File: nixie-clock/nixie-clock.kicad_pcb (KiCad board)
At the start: 2 copper layers, 184 x 105 mm, 63 parts, among them J1 Barrel_Jack_Switch, J2 Conn_01x08, J3 Conn_01x06, J4 AVR-ISP-6, SW1 SW_Push, SW2 SW_Push, SW3 SW_Push, SW4 SW_Push, U1 NCH6100HV, U10 74HC595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

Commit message: Add some extra silkscreen stuff.
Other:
- board text added: "IN-1"
- board text added: "IN-12"
- board text added: "IN-2"
- board text added: "IN-3"
- board text added: "IN1, IN12, IN2, IN3 Nixie Clock Nathan Aquino Dornback ndornback@gmail.com April 24th, 2020"
- board text removed: "IN1, IN12, IN2, IN3 Nixie Clock Nathan Aquino Dornback April 24th, 2020"
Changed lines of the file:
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@@
   (general
     (thickness 1.6)
-    (drawings 67)
+    (drawings 75)
     (tracks 1456)
     (zones 0)
@@
     (39 F.Mask user)
     (40 Dwgs.User user)
-    (41 Cmts.User user hide)
+    (41 Cmts.User user)
     (42 Eco1.User user)
     (43 Eco2.User user)
@@
       (effects (font (size 1.27 1.27) (thickness 0.1016)))
     )
-    (fp_text value IN-3 (at 0 0) (layer F.SilkS)
+    (fp_text value IN-3 (at 0 -5) (layer F.SilkS) hide
       (effects (font (size 1.27 1.27) (thickness 0.15)))
     )
@@
       (effects (font (size 1.27 1.27) (thickness 0.1016)))
     )
-    (fp_text value IN-3 (at 0 0) (layer F.SilkS)
+    (fp_text value IN-3 (at 0 0) (layer F.SilkS) hide
       (effects (font (size 1.27 1.27) (thickness 0.15)))
     )
@@
       (effects (font (size 1.27 1.27) (thickness 0.1016)))
     )
-    (fp_text value IN-12A (at 0 0) (layer F.SilkS)
+    (fp_text value IN-12A (at 0 -4.129158) (layer F.SilkS) hide
       (effects (font (size 1.27 1.27) (thickness 0.15)))
     )
-    (fp_text user Top (at 0.635 -5.715) (layer F.SilkS)
-      (effects (font (size 1.27 1.27) (thickness 0.1016)))
-    )
-    (fp_text user Bot (at 0.635 5.715) (layer F.SilkS)
+    (fp_text user Bot (at 0.225567 5.715) (layer F.SilkS)
       (effects (font (size 1.27 1.27) (thickness 0.1016)))
     )
@@
       (effects (font (size 1.27 1.27) (thickness 0.1016)))
     )
-    (fp_text value IN-12A (at 0 0) (layer F.SilkS)
+    (fp_text value IN-12A (at 0 0) (layer F.SilkS) hide
       (effects (font (size 1.27 1.27) (thickness 0.15)))
     )
-    (fp_text user Top (at 0.635 -5.715) (layer F.SilkS)
-      (effects (font (size 1.27 1.27) (thickness 0.1016)))
-    )
-    (fp_text user Bot (at 0.635 5.715) (layer F.SilkS)
+    (fp_text user Bot (at 0.135567 5.715) (layer F.SilkS)
       (effects (font (size 1.27 1.27) (thickness 0.1016)))
     )
@@
     )
   )
+  (gr_text IN-3 (at 166 101.5) (layer F.SilkS)
+    (effects (font (size 1 1) (thickness 0.15)))
+  )
+  (gr_text IN-3 (at 114 101.5) (layer F.SilkS)
+    (effects (font (size 1 1) (thickness 0.15)))
+  )
+  (gr_text IN-12 (at 129.5 110.5) (layer F.SilkS)
+    (effects (font (size 1 1) (thickness 0.15)))
+  )
+  (gr_text IN-12 (at 150.5 110.5) (layer F.SilkS)
+    (effects (font (size 1 1) (thickness 0.15)))
+  )
+  (gr_text IN-1 (at 88 115) (layer F.SilkS)
+    (effects (font (size 3 3) (thickness 0.45)))
+  )
+  (gr_text IN-1 (at 50 115) (layer F.SilkS)
+    (effects (font (size 3 3) (thickness 0.45)))
+  )
+  (gr_text IN-2 (at 199 115) (layer F.SilkS)
+    (effects (font (size 1 1) (thickness 0.15)))
+  )
+  (gr_text IN-2 (at 180 115) (layer F.SilkS)
+    (effects (font (size 1 1) (thickness 0.15)))
+  )
   (dimension 105 (width 0.15) (layer Dwgs.User)
     (gr_text "105.000 mm" (at 217.3 82.5 90) (layer Dwgs.User)
@@
     (arrow2b (pts (xy 124 131) (xy 125.126504 130.413579)))
   )
-  (gr_text "IN1, IN12, IN2, IN3 Nixie Clock\nNathan Aquino Dornback\nApril 24th, 2020" (at 203 126) (layer B.SilkS)
+  (gr_text "IN1, IN12, IN2, IN3 Nixie Clock\nNathan Aquino Dornback\nndornback@gmail.com\nApril 24th, 2020\n" (at 203 126) (layer B.SilkS)
     (effects (font (size 1 1) (thickness 0.15)) (justify left mirror))
   )

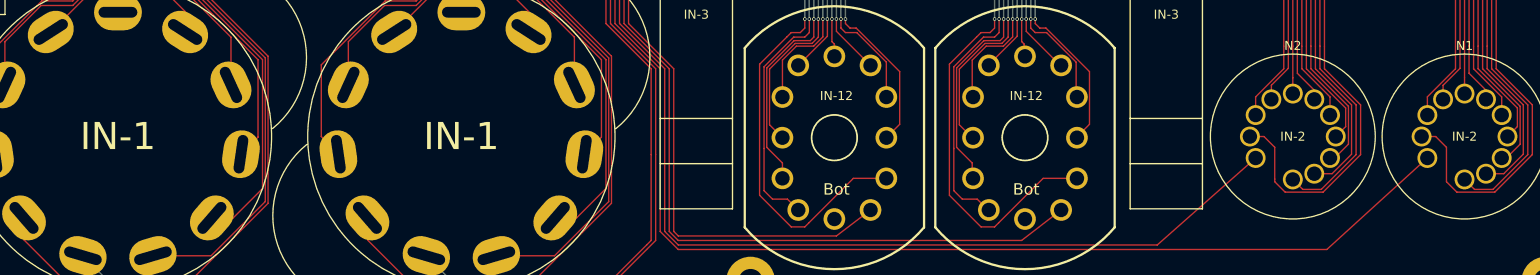
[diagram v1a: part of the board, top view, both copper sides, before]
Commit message: Added several image footprints. Added to nixie-clock silkscreen.
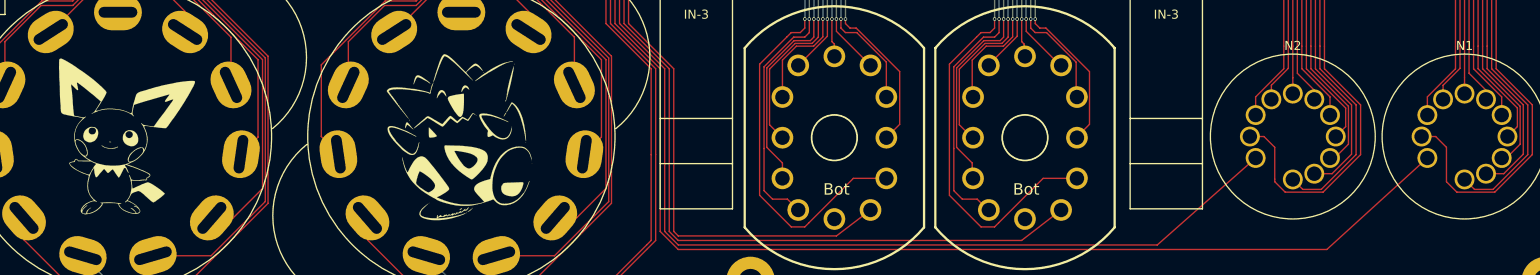
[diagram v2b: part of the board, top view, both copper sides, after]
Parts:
- added G***: LOGO, footprints-nad:pichu1, F.Cu at (51.0, 115.0)
- added G***: LOGO, footprints-nad:togepi1, F.Cu at (88.0, 115.0)

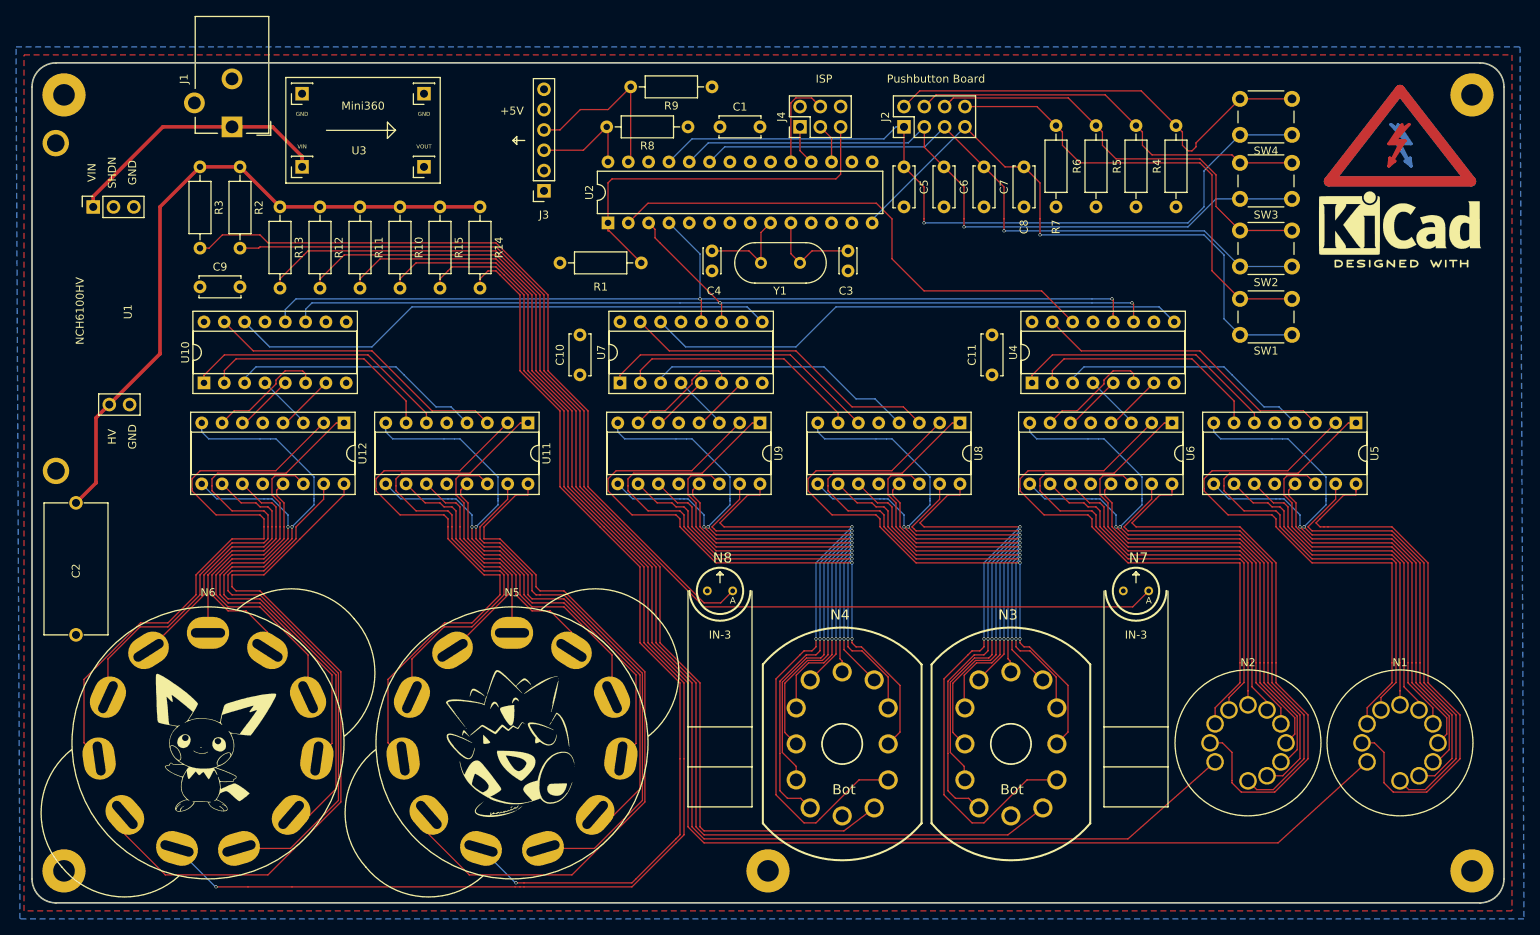
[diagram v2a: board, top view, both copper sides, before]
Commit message: Added res/cap values to silkscreen and more adjustments. Added footprint-tester board sent to OSHPARK.
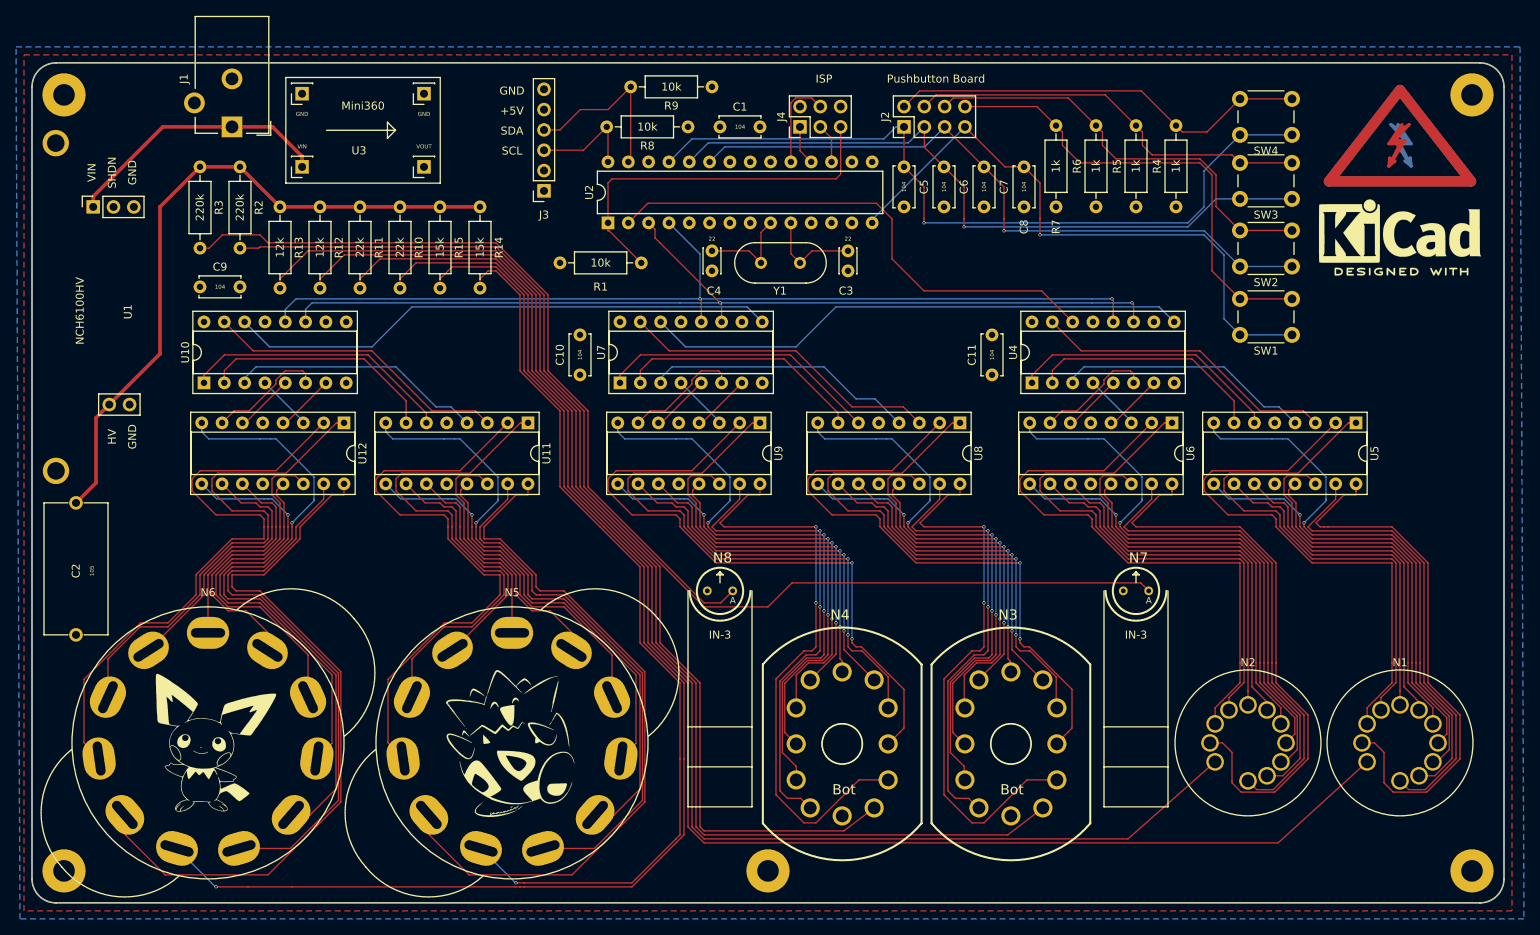
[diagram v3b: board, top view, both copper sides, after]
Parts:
- moved REF** 1.00 mm to (199.0, 51.0)
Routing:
- net /shiftout/N3_0: track 76.3 -> 69.9 mm
- net /shiftout/N4_0: track 80.3 -> 73.9 mm
- net /shiftout/N4_1: track 66.1 -> 60.5 mm
- net /shiftout/N3_1: track 62.1 -> 56.5 mm
- net /shiftout/N4_2: track 79.3 -> 74.3 mm
- net /shiftout/N3_2: track 75.3 -> 70.3 mm
- net /shiftout/N4_3: track 63.8 -> 59.6 mm
- net /shiftout/N3_3: track 59.8 -> 55.6 mm
- net /shiftout/N4_4: track 50.6 -> 47.0 mm
- net /shiftout/N3_4: track 46.6 -> 43.0 mm
- net Net-(J2-Pad2): track 56.4 -> 53.2 mm
- net /shiftout/N3_5: track 46.3 -> 43.4 mm
- net /shiftout/N4_5: track 50.3 -> 47.4 mm
- net /shiftout/N4_6: track 45.0 -> 42.9 mm
- net /shiftout/N3_6: track 41.0 -> 38.9 mm
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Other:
- board text added: "104"
- board text added: "105"
- board text added: "22"
- board text added: "GND"
- board text added: "Grid: 1mm Routing Grid: 0.5mm Normal Trace Width: 6 mils Power Trace Width: 18 mils"
- board text added: "Nixie Clock"
- board text added: "SCL"
- board text added: "SDA"
- board text added: "Yours truly, Nathan Aquino Dornback April 24th, 2020"
- board text added: "ndornback@gmail.com"
- board text removed: "IN1, IN12, IN2, IN3 Nixie Clock Nathan Aquino Dornback ndornback@gmail.com April 24th, 2020"
